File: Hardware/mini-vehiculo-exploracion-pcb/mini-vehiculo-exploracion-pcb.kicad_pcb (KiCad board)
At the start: 4 copper layers, 92 x 67 mm, 84 parts, among them IC3 MAX8891EXK33_V+T, J1 CÁMARA, J3 UJ20-C-H-G-SMT-5-P16-TR, J8 SERVO, Q1 SI1467DH-T1-BE3, U2 ESP32-S3-WROOM-1, U3 LM358, U4 TPS561208DDCR

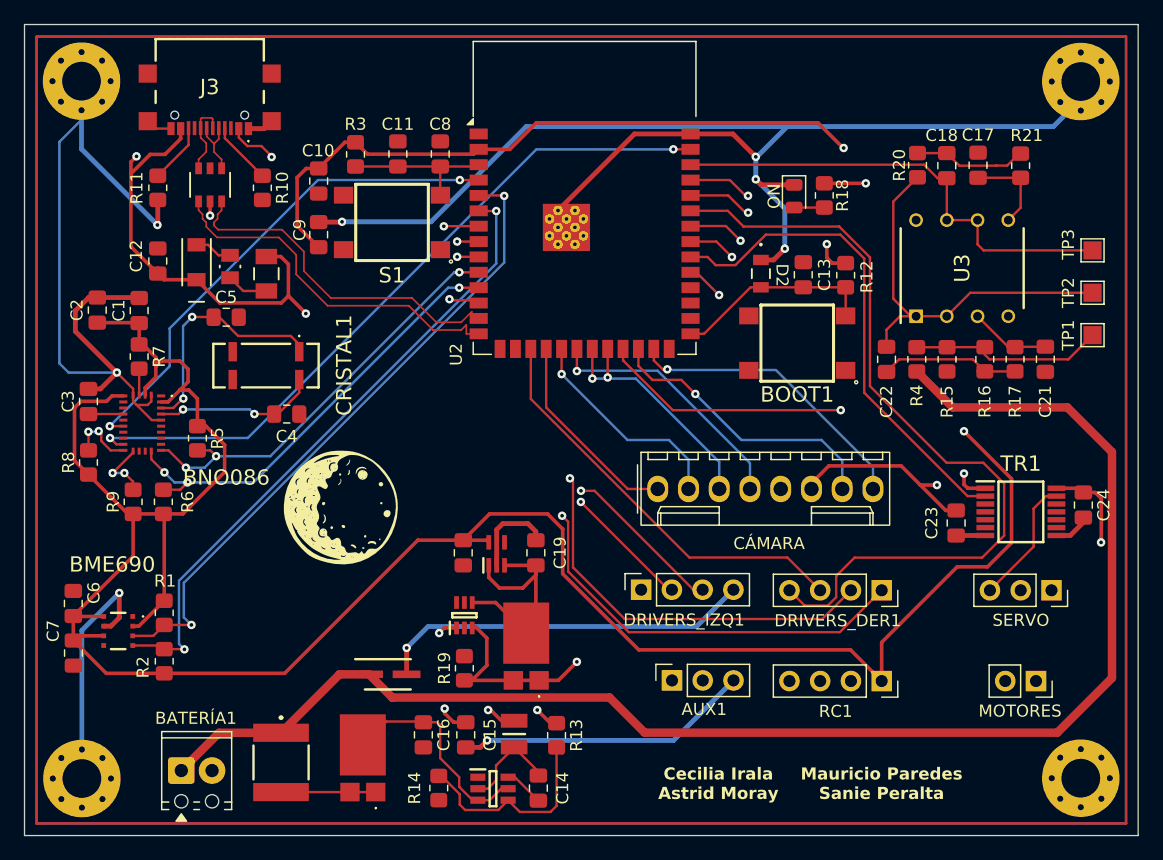
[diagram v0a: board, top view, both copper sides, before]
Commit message: add vias
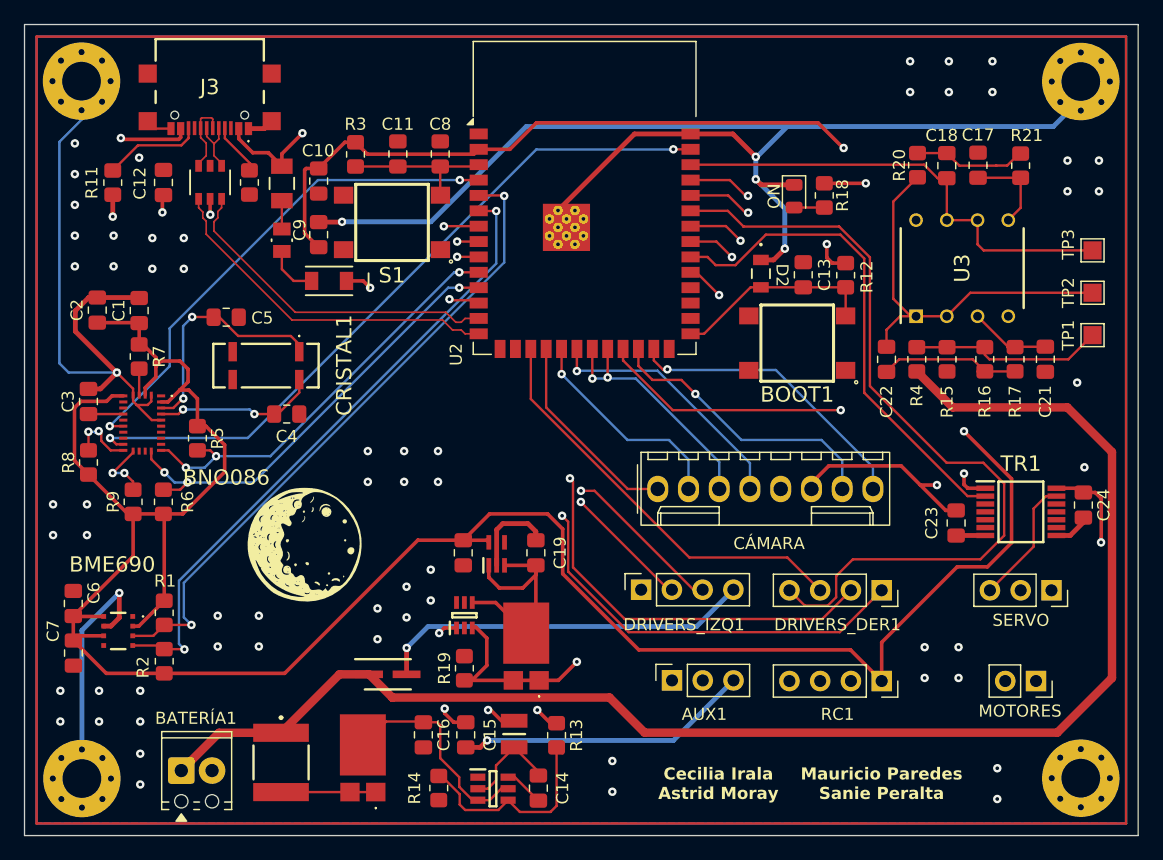
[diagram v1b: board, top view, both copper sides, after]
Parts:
- moved D1 11.1 mm to (110.0, 63.0), turned to 180 degrees
- moved F1 7.57 mm to (106.1, 55.0)
- moved C12 6.50 mm to (96.3, 54.9)
- moved FB1 4.80 mm to (106.1, 59.6), turned to -90 degrees
- moved G*** 4.29 mm to (108.0, 84.8)
- moved R11 3.74 mm to (92.1, 54.9)
- moved R10 1.16 mm to (103.4, 54.9)
- moved CR1 0.21 mm to (100.2, 54.9)
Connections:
- F1 pad 1: V_BUS -> /MCU_Peripherals/V_BUS1
- J3 pad A4: V_BUS -> /MCU_Peripherals/V_BUS1
- J3 pad B4: V_BUS -> /MCU_Peripherals/V_BUS1
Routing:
- net V_BUS: track 115.3 -> 80.9 mm, vias 5 -> 4
- net /MCU_Peripherals/V_BUS1: track 0.00 -> 30.6 mm, vias 0 -> 2
- net GND: track 267.9 -> 255.5 mm, vias 9 -> 69
- net /MCU_Peripherals/CC2: track 4.98 -> 8.19 mm
- net USB_D-: track 29.3 -> 28.0 mm
- net Net-(D1-A): track 3.13 -> 4.32 mm
- net USB_D+: track 30.7 -> 29.6 mm
- net Net-(F1-Pad2): track 3.45 -> 2.34 mm
- net /MCU_Peripherals/CC1: track 5.21 -> 4.40 mm
- net +3.3V: track 316.8 -> 316.3 mm

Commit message: innit fix edgecut
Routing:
- removed copper zone on F.Cu, net GND
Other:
- board size 92 x 67 mm -> 194.6 x 92.6 mm

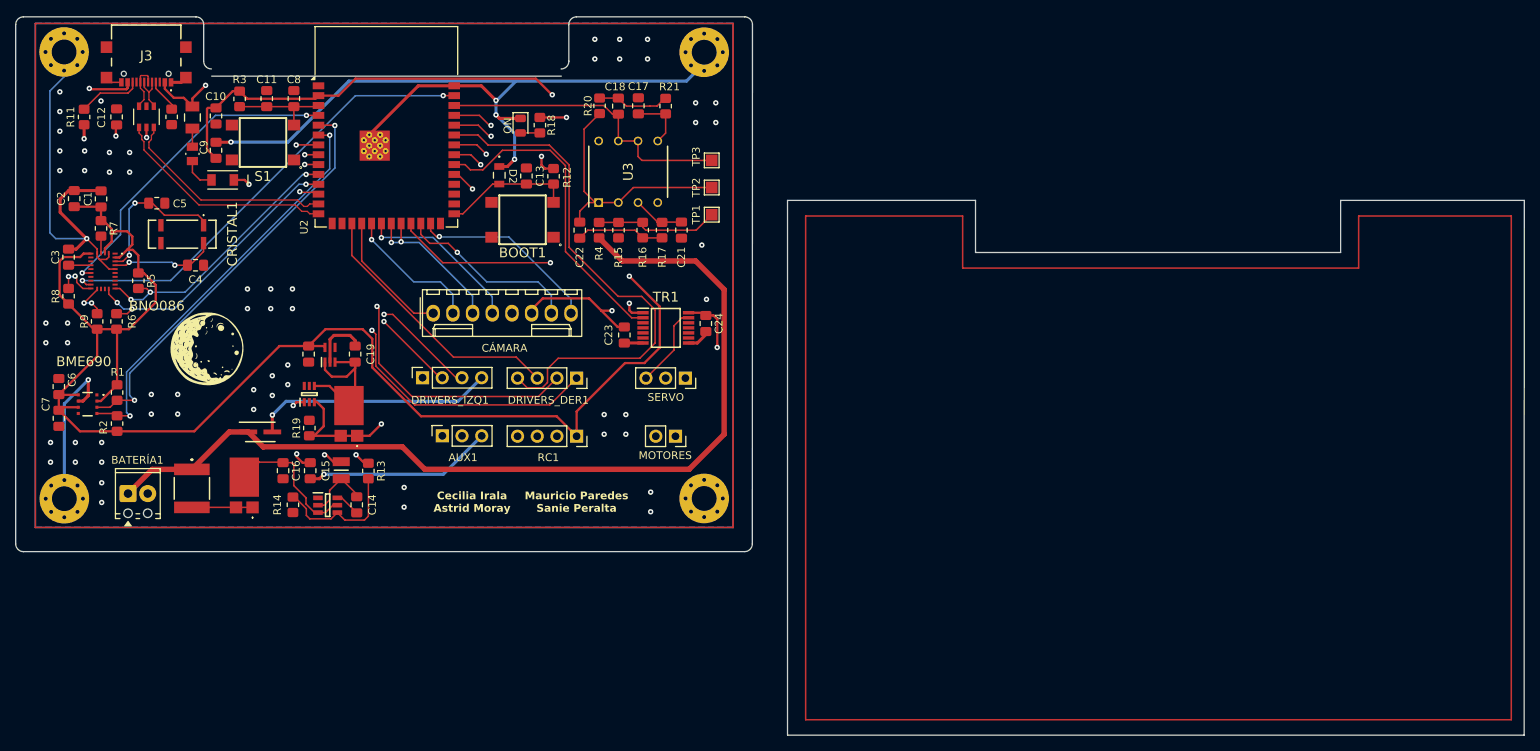
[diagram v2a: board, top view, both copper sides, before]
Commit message: fin adapt edgecuts
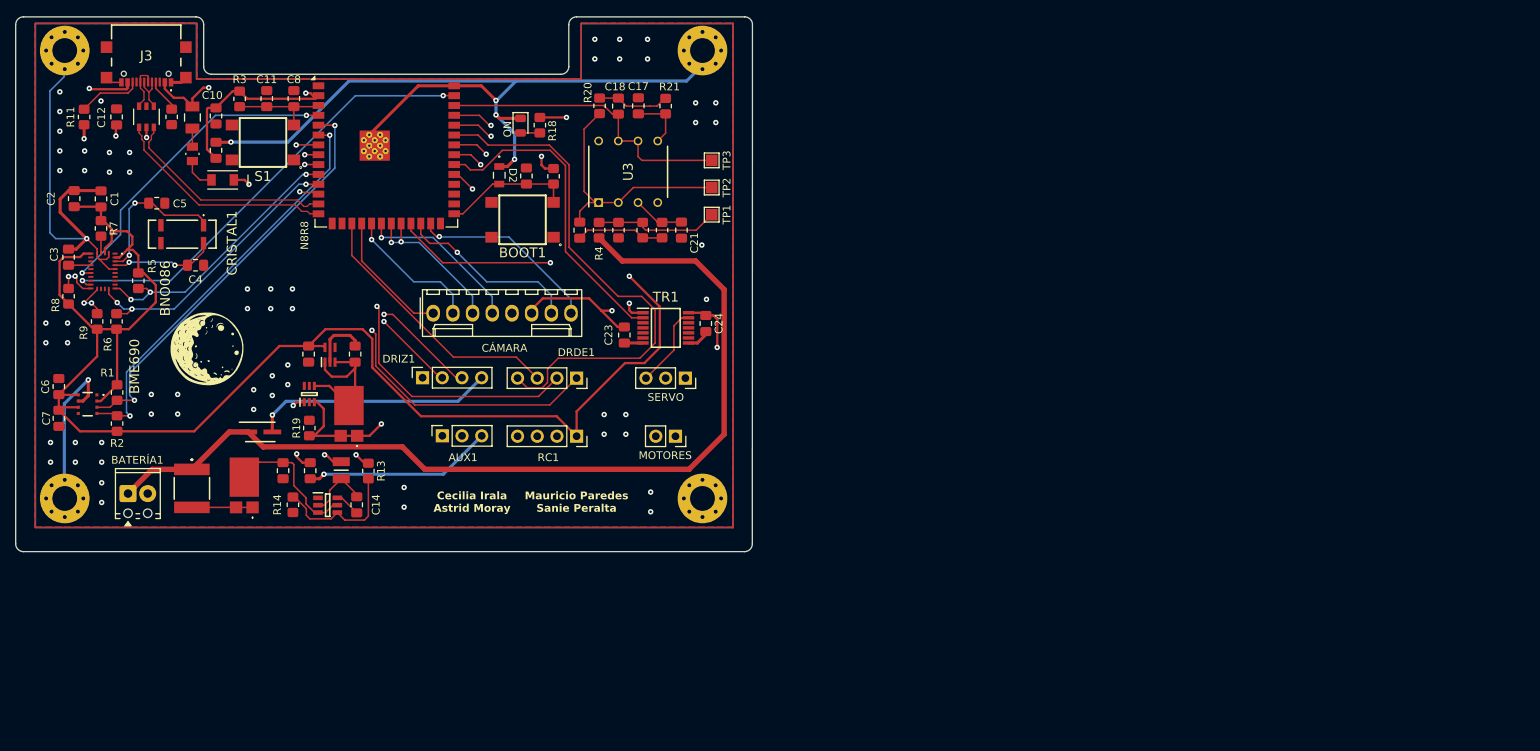
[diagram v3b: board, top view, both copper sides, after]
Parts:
- moved H2 0.31 mm to (171.9, 46.3)
- moved H3 0.22 mm to (171.9, 104.1)
- moved H1 0.20 mm to (89.6, 46.3)
- moved H4 0.06 mm to (89.6, 104.1)
- renumbered DRIVERS_DER1 to DRDE1, DRIVERS_IZQ1 to DRIZ1, U2 to N8R8
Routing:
- net +3.3V: track 316.3 -> 319.3 mm
- net /MCU_Peripherals/V_BUS1: track 30.6 -> 31.2 mm
- added copper zone on F.Cu, net GND
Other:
- board size 194.6 x 92.6 mm -> 95 x 69 mm

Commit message: Changed 3v3 dist
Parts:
- moved C3 0.92 mm to (89.2, 73.0)
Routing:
- net +3.3V: track 319.3 -> 140.6 mm, vias 6 -> 19
- net GND: track 255.5 -> 245.9 mm, vias 69 -> 86
- net Net-(BNO086-ENV_SDA): track 5.16 -> 3.19 mm, vias 2 -> 0
- net /TX_1: track 35.3 -> 33.4 mm, vias 3 -> 2
- net Net-(BNO086-CAP): track 2.88 -> 3.80 mm
- net /RX_1: track 37.4 -> 36.6 mm, vias 3 -> 2
- net /XTAL_N: track 13.5 -> 13.2 mm, vias 2 -> 0
- net /XTAL_P: track 19.6 -> 19.5 mm, vias 2 -> 0

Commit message: Add gnds
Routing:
- net +3.3V: track 140.6 -> 131.9 mm
- net Net-(BNO086-ENV_SCL): track 5.61 -> 2.88 mm, vias 2 -> 0
- net /M2_IN2: track 41.1 -> 42.3 mm
- net GND: track 245.9 -> 245.7 mm, vias 86 -> 123

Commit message: edit1
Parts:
- removed G***: LOGO, Assets:luna1
- moved R19 1.54 mm to (120.8, 93.5), turned to 180 degrees
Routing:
- net V_BUS: track 80.9 -> 77.1 mm
- net +3.3V: track 131.9 -> 130.2 mm
- net GND: vias 123 -> 128

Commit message: add luna
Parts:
- added G***: LOGO, luna_sailormoon, F.Cu at (108.5, 87.8)
